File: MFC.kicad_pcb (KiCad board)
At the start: 2 copper layers, 101.6 x 53.3 mm, 30 parts, among them J1 DB15_Female_MountingHoles, J10 Conn_01x01_Male, J11 Conn_01x01_Male, J12 Conn_01x01_Male, J2 Conn_01x04_Male, J4 647676-3, J5 Conn_01x01_Male, J6 Conn_01x01_Male

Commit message: Update to KiCad 7
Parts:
- DACss0, J10, J11, J12, J5, J6: value Conn_01x01_Male -> Conn_01x01_Pin
- J1: value DB15_Female_MountingHoles -> DA15_Receptacle_MountingHoles
- J2: value Conn_01x04_Male -> Conn_01x04_Pin

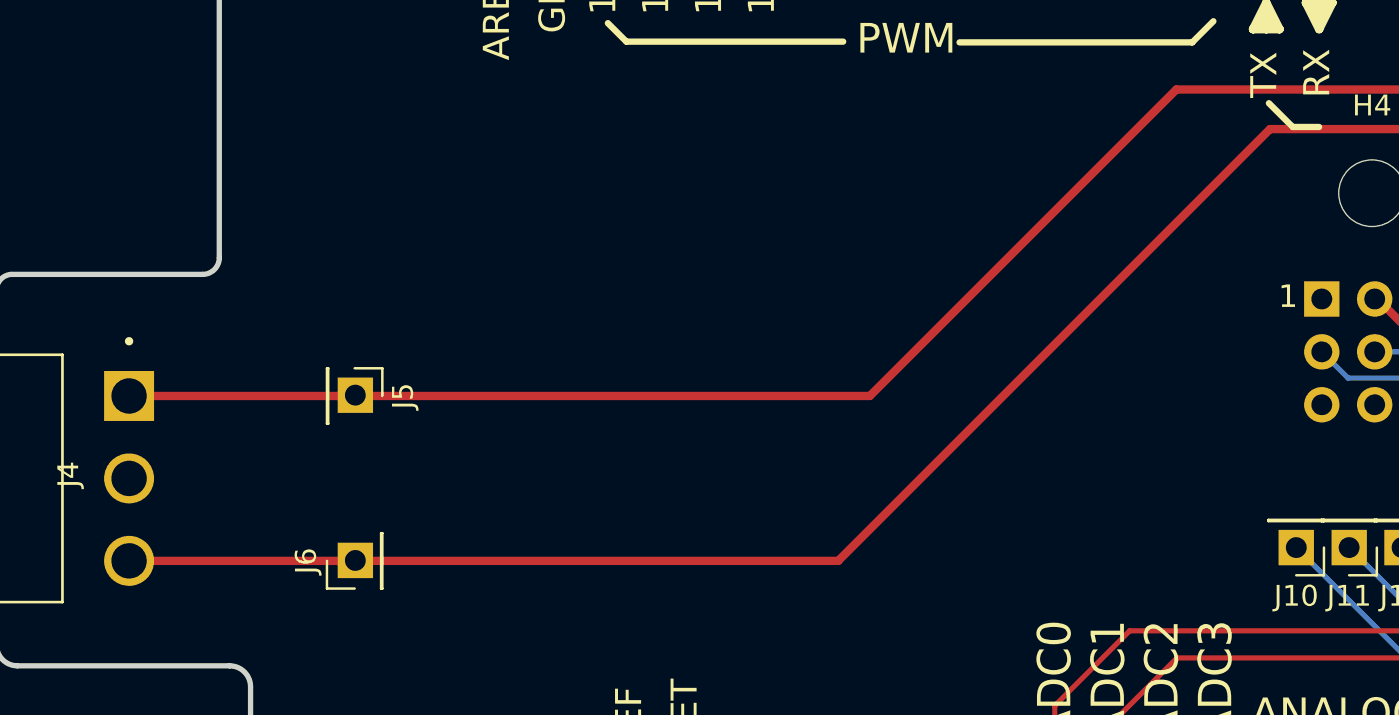
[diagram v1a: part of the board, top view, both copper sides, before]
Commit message: Reduced space between +15 and -15 transversal header to fit 5.08 connectors
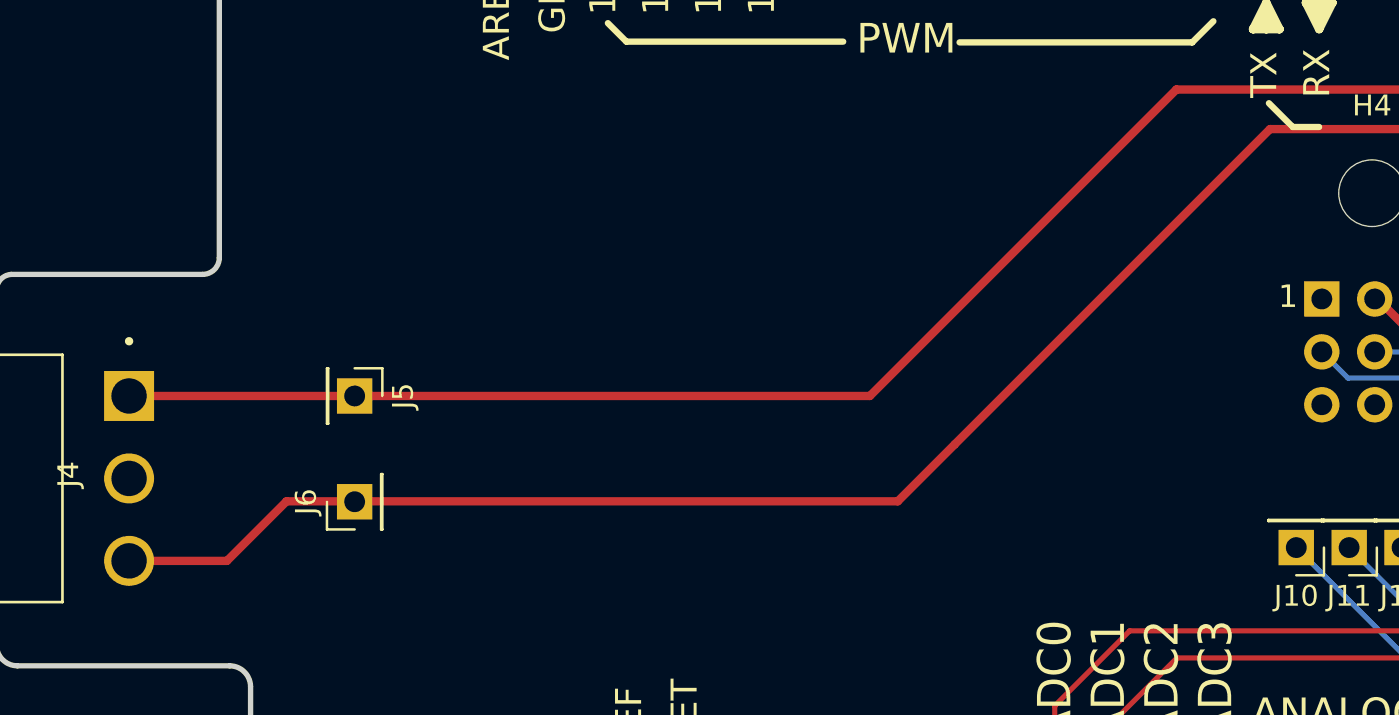
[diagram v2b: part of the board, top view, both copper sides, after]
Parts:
- moved J6 2.84 mm to (104.2, 101.8)
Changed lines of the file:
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@@
   )
   (footprint "Connector_PinHeader_2.54mm:PinHeader_1x01_P2.54mm_Vertical" (layer "F.Cu")
-    (at 104.2344 104.6392 90)
+    (at 104.2344 101.7992 90)
     (descr "Through hole straight pin header, 1x01, 2.54mm pitch, single row")
     (tags "Through hole pin header THT 1x01 2.54mm single row")
@@
     (fp_line (start 1.27 1.27) (end -1.27 1.27)
       (stroke (width 0.1) (type solid)) (layer "F.Fab"))
-    (pad "1" thru_hole rect (at 0.020707 0.032893 90) (size 1.7 1.7) (drill 1) (layers "F&B.Cu" "*.Mask")
+    (pad "1" thru_hole rect (at 0 0 90) (size 1.7 1.7) (drill 1) (layers "*.Cu" "*.Mask")
       (net 24 "-15V") (pinfunction "Pin_1") (pintype "passive"))
     (model "${KICAD6_3DMODEL_DIR}/Connector_PinHeader_2.54mm.3dshapes/PinHeader_1x01_P2.54mm_Vertical.wrl"
@@
     (fp_line (start 1.27 1.27) (end -1.27 1.27)
       (stroke (width 0.1) (type solid)) (layer "F.Fab"))
-    (pad "1" thru_hole rect (at -0.040707 -0.032893 270) (size 1.7 1.7) (drill 1) (layers "F&B.Cu" "*.Mask")
+    (pad "1" thru_hole rect (at 0 0 270) (size 1.7 1.7) (drill 1) (layers "*.Cu" "*.Mask")
       (net 23 "+15V") (pinfunction "Pin_1") (pintype "passive"))
     (model "${KICAD6_3DMODEL_DIR}/Connector_PinHeader_2.54mm.3dshapes/PinHeader_1x01_P2.54mm_Vertical.wrl"
@@
   (segment (start 177.783369 86.2) (end 175.9625 86.2) (width 0.4) (layer "B.Cu") (net 23))
   (segment (start 175.9625 84.7) (end 175.9625 86.2) (width 0.4) (layer "B.Cu") (net 23))
-  (segment (start 148.2 83.9) (end 127.4608 104.6392) (width 0.4) (layer "F.Cu") (net 24))
-  (segment (start 127.4608 104.6392) (end 93.4 104.6392) (width 0.4) (layer "F.Cu") (net 24))
+  (segment (start 98.1 104.6392) (end 100.960707 101.778493) (width 0.4) (layer "F.Cu") (net 24))
+  (segment (start 98.1 104.6392) (end 93.4 104.6392) (width 0.4) (layer "F.Cu") (net 24))
+  (segment (start 104.267293 101.778493) (end 130.321507 101.778493) (width 0.4) (layer "F.Cu") (net 24))
+  (segment (start 130.321507 101.778493) (end 133.05 99.05) (width 0.4) (layer "F.Cu") (net 24))
+  (segment (start 100.960707 101.778493) (end 104.267293 101.778493) (width 0.4) (layer "F.Cu") (net 24))
   (segment (start 168.47 88.97) (end 163.4 83.9) (width 0.4) (layer "F.Cu") (net 24))
+  (segment (start 148.2 83.9) (end 133.05 99.05) (width 0.4) (layer "F.Cu") (net 24))
   (segment (start 163.4 83.9) (end 148.2 83.9) (width 0.4) (layer "F.Cu") (net 24))
   (segment (start 177.783369 88.97) (end 168.47 88.97) (width 0.4) (layer "F.Cu") (net 24))

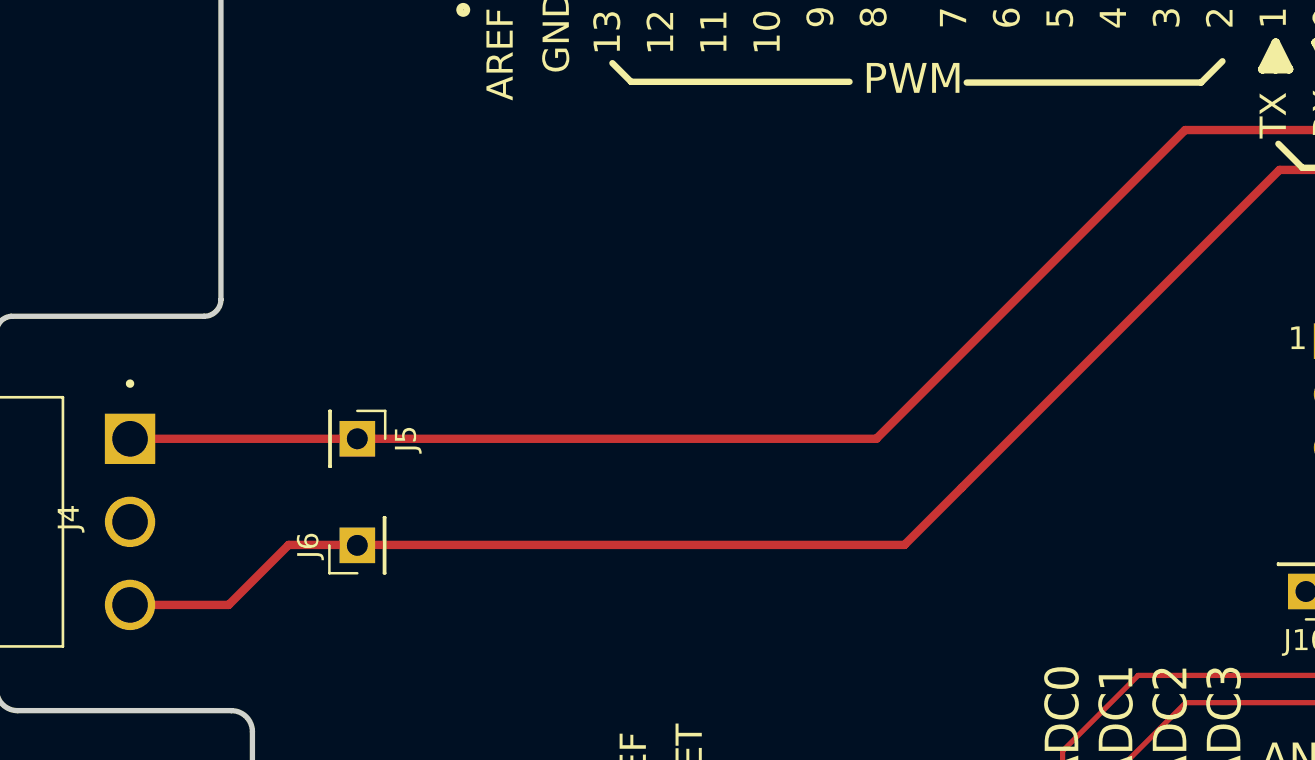
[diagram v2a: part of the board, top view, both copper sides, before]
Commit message: Changed transversal power connector
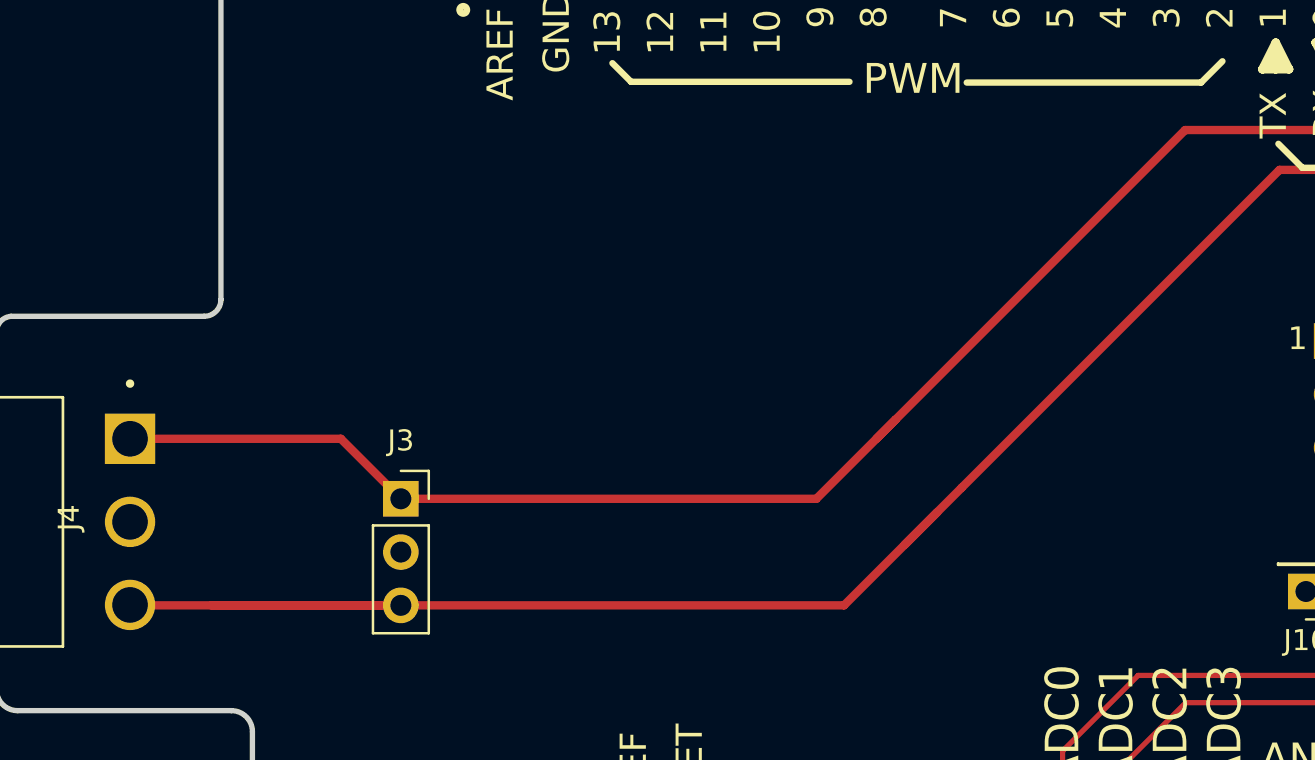
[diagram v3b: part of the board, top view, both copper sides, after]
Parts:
- removed J5, J6: Conn_01x01_Pin, Connector_PinHeader_2.54mm:PinHeader_1x01_P2.54mm_Vertical
- added J3: Conn_01x03_Socket, Connector_PinSocket_2.54mm:PinSocket_1x03_P2.54mm_Vertical, F.Cu at (106.3, 99.6)
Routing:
- net -15V: track 98.4 -> 109.7 mm
- net +15V: track 95.5 -> 99.2 mm

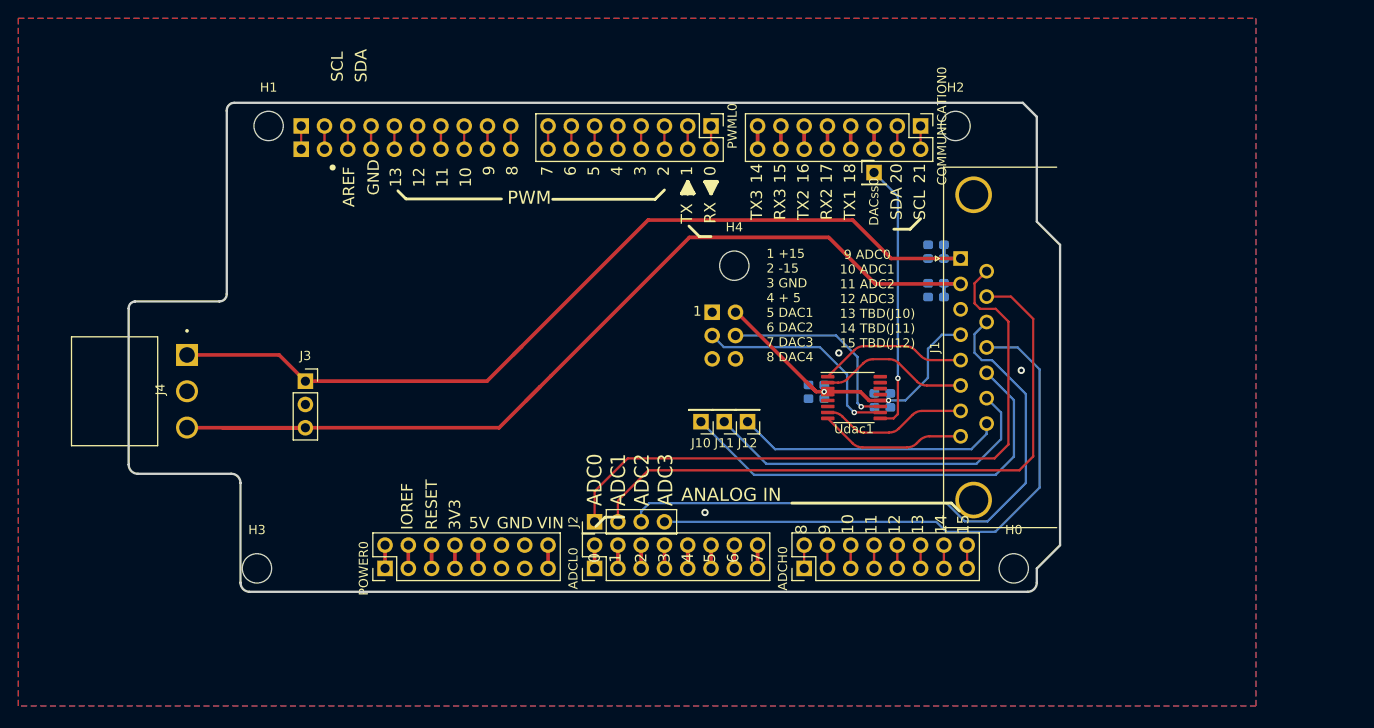
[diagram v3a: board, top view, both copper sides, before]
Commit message: Added MAX232 Optimised DAC8554 Routing
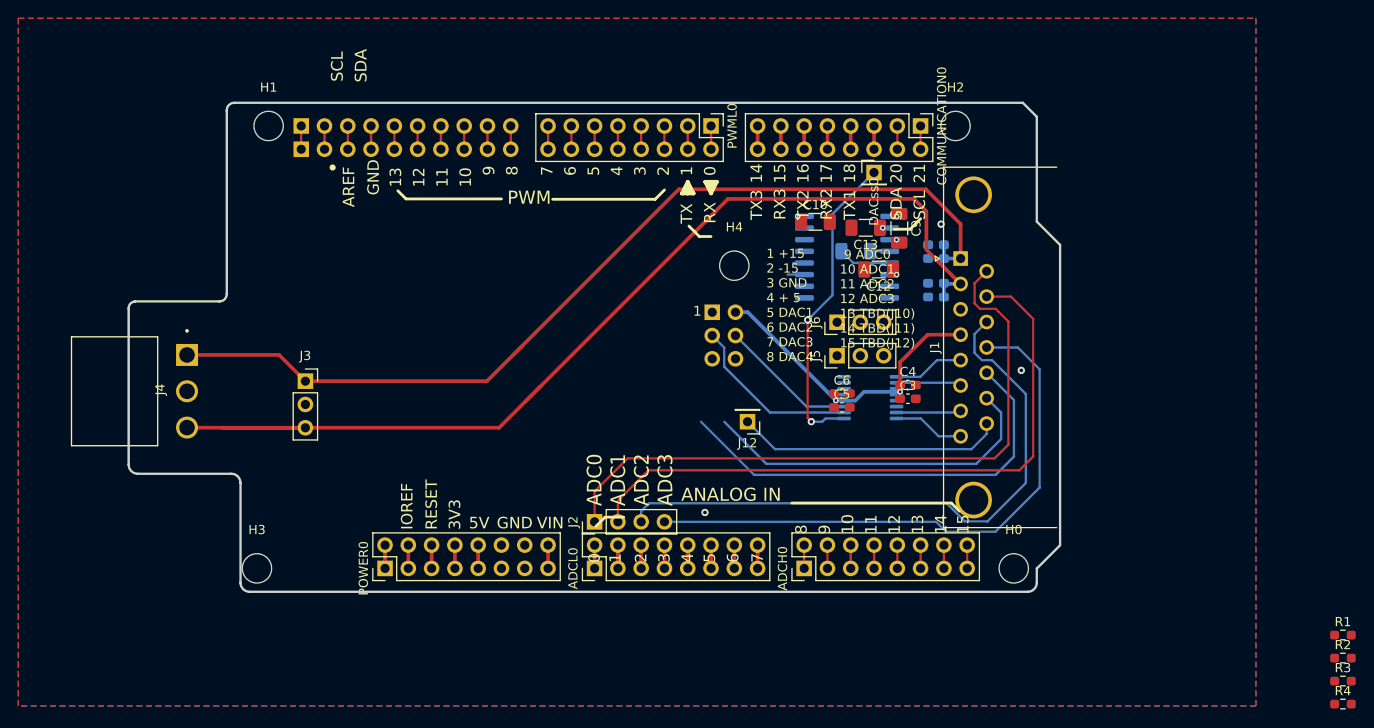
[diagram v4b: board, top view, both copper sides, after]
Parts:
- removed J10, J11: Conn_01x01_Pin, Connector_PinHeader_2.54mm:PinHeader_1x01_P2.54mm_Vertical
- added C10: 1µF, Capacitor_SMD:C_1206_3216Metric_Pad1.33x1.80mm_HandSolder, F.Cu at (161.9, 82.2)
- added C11: 1µF, Capacitor_SMD:C_1206_3216Metric_Pad1.33x1.80mm_HandSolder, B.Cu at (166.3, 85.4)
- added C12: 1µF, Capacitor_SMD:C_1206_3216Metric_Pad1.33x1.80mm_HandSolder, F.Cu at (168.8, 87.4)
- added C13: 1µF, Capacitor_SMD:C_1206_3216Metric_Pad1.33x1.80mm_HandSolder, F.Cu at (167.4, 82.8)
- added C9: 1µF, Capacitor_SMD:C_1206_3216Metric_Pad1.33x1.80mm_HandSolder, F.Cu at (171.1, 82.9)
- added J5: Conn_01x03_Pin, Connector_PinHeader_2.54mm:PinHeader_1x03_P2.54mm_Vertical, F.Cu at (164.3, 96.8)
- added J6: Conn_01x03_Pin, Connector_PinHeader_2.54mm:PinHeader_1x03_P2.54mm_Vertical, F.Cu at (164.3, 93.2)
- added R1: 0, Resistor_SMD:R_0603_1608Metric_Pad0.98x0.95mm_HandSolder, F.Cu at (219.5, 127.3)
- added R2: R, Resistor_SMD:R_0603_1608Metric_Pad0.98x0.95mm_HandSolder, F.Cu at (219.5, 129.8)
- added R3: 0, Resistor_SMD:R_0603_1608Metric_Pad0.98x0.95mm_HandSolder, F.Cu at (219.5, 132.3)
- added R4: R, Resistor_SMD:R_0603_1608Metric_Pad0.98x0.95mm_HandSolder, F.Cu at (219.5, 134.8)
- added U1: MAX232, Package_SO:SOIC-16W_7.5x10.3mm_P1.27mm, B.Cu at (165.4, 86.0)
- C3, C4, C5, C6: moved to F.Cu
- Udac1: moved to B.Cu
- moved C3 9.98 mm to (172.0, 101.5), turned to 0 degrees
- moved C4 9.98 mm to (172.0, 100.0), turned to 0 degrees
- moved C5 4.42 mm to (164.8, 102.4), turned to 0 degrees
- moved C6 4.40 mm to (164.8, 100.9), turned to 0 degrees
- moved Udac1 1.78 mm to (167.9, 101.4), turned to 180 degrees
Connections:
- J1 pad 13: Net-(J1-P13) -> /Serial_MOSI
- J1 pad 14: Net-(J1-P14) -> /Serial_MISO
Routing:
- net Net-(J1-P13): track 47.7 -> 0.00 mm
- net /Serial_MOSI: track 0.00 -> 47.7 mm
- net Net-(J1-P14): track 38.3 -> 0.00 mm
- net /Serial_MISO: track 0.00 -> 38.3 mm
- net /DAC_{2}: track 16.4 -> 7.11 mm
- net /DAC_{3}: track 16.1 -> 7.06 mm
- net /DAC_{1}: track 16.3 -> 7.74 mm
- net /DAC_{4}: track 16.1 -> 7.79 mm
- net /MOSI: track 22.0 -> 15.1 mm, vias 1 -> 0
- net -15V: track 109.7 -> 115.6 mm
- net Net-(U1-C2-): track 0.00 -> 5.79 mm
- net +15V: track 99.2 -> 104.2 mm
- net /PB1: track 23.8 -> 19.1 mm, vias 1 -> 0
- net /SS: track 29.5 -> 34.1 mm, vias 1 -> 2
- net Net-(U1-C2+): track 0.00 -> 2.14 mm
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
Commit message: First routing done
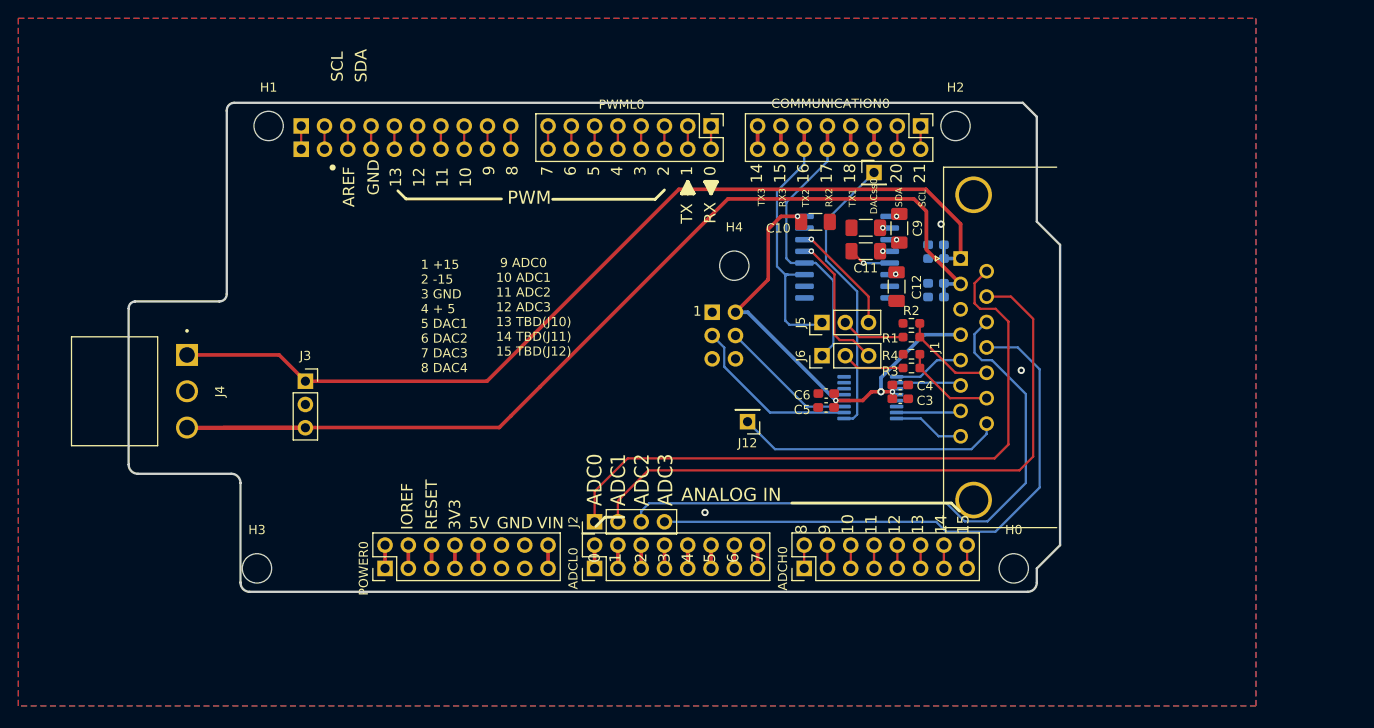
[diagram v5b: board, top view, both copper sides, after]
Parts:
- C11: moved to F.Cu
- moved R4 60.6 mm to (172.4, 96.6), turned to 180 degrees
- moved R2 59.6 mm to (172.4, 93.3), turned to 180 degrees
- moved R3 58.1 mm to (172.4, 98.1)
- moved R1 57.2 mm to (172.4, 94.8)
- moved J6 4.00 mm to (162.7, 96.8)
- moved J5 3.98 mm to (162.7, 93.2)
- moved C12 2.70 mm to (170.8, 89.3), turned to -90 degrees
- moved C5 1.72 mm to (163.1, 102.4), turned to 180 degrees
- moved C6 1.72 mm to (163.1, 100.9), turned to 180 degrees
- moved C11 1.09 mm to (167.4, 85.4)
- moved C3 0.84 mm to (171.2, 101.5)
- moved C4 0.84 mm to (171.2, 100.0)
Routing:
- net /Serial_MOSI: track 47.7 -> 10.4 mm
- net /Serial_MISO: track 38.3 -> 10.1 mm
- net /RXD2: track 3.76 -> 31.1 mm
- net /TXD2: track 4.39 -> 29.5 mm
- net /RS232_MISO: track 0.00 -> 14.8 mm, vias 0 -> 1
- net +5V: track 37.5 -> 52.1 mm, vias 3 -> 4
- net /RS232_MOSI: track 0.00 -> 11.7 mm, vias 0 -> 1
- net -15V: track 115.6 -> 126.3 mm
- net Net-(J5-Pin_2): track 0.00 -> 6.96 mm
- net Net-(J6-Pin_2): track 0.00 -> 6.86 mm
- net /SS: track 34.1 -> 31.6 mm, vias 2 -> 0
- net Net-(U1-C2+): track 2.14 -> 0.00 mm, vias 0 -> 1
- net +15V: track 104.2 -> 102.9 mm
- net Net-(U1-C2-): track 5.79 -> 4.72 mm, vias 0 -> 1
